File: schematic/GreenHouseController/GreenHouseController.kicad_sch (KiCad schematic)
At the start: 7 parts, among them J1 Conn_01x05, J2 Conn_01x02, J3 Conn_01x02, Q1 AO3400A, Q2 AO3400A, U1 ESP32-WROOM-32

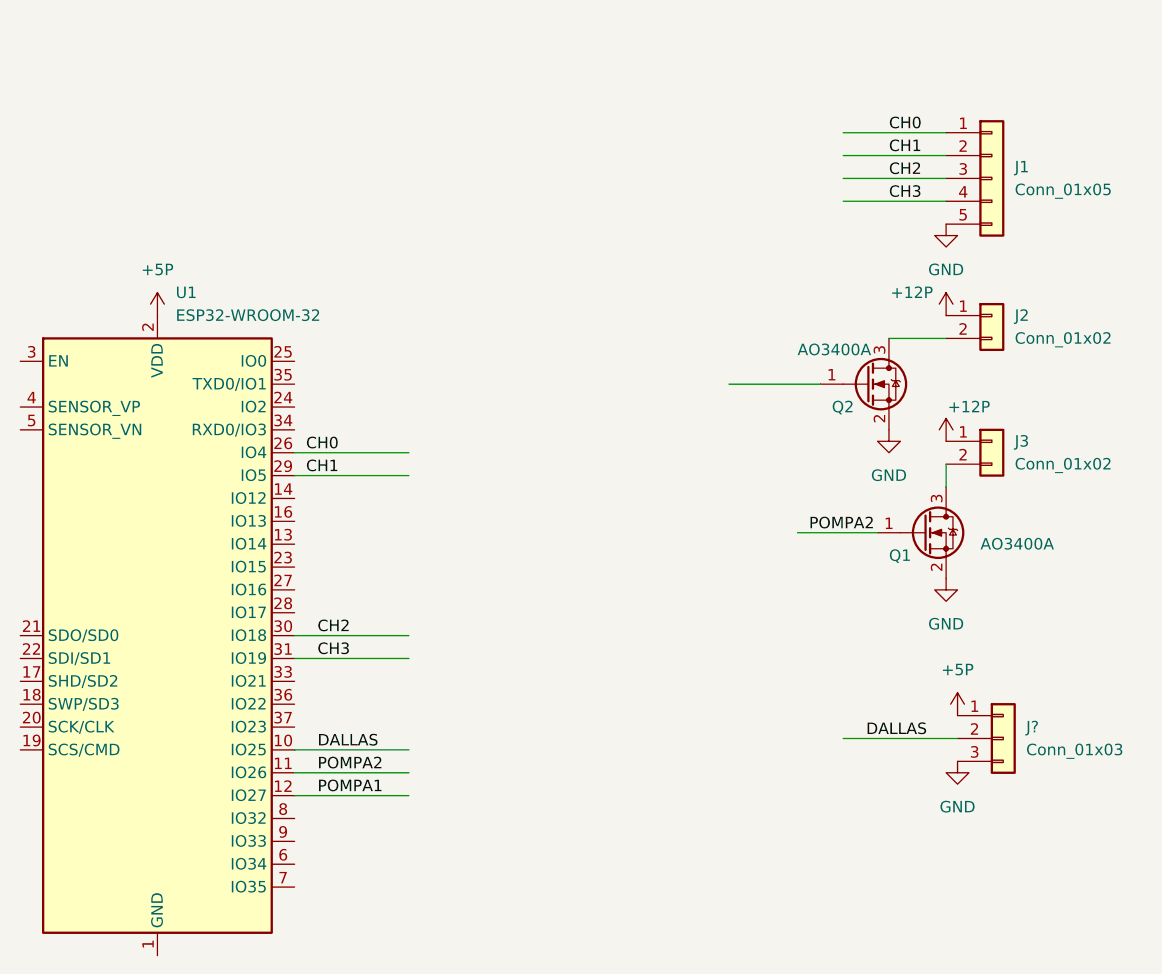
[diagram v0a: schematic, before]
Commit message: Inverted CH0-4 signals
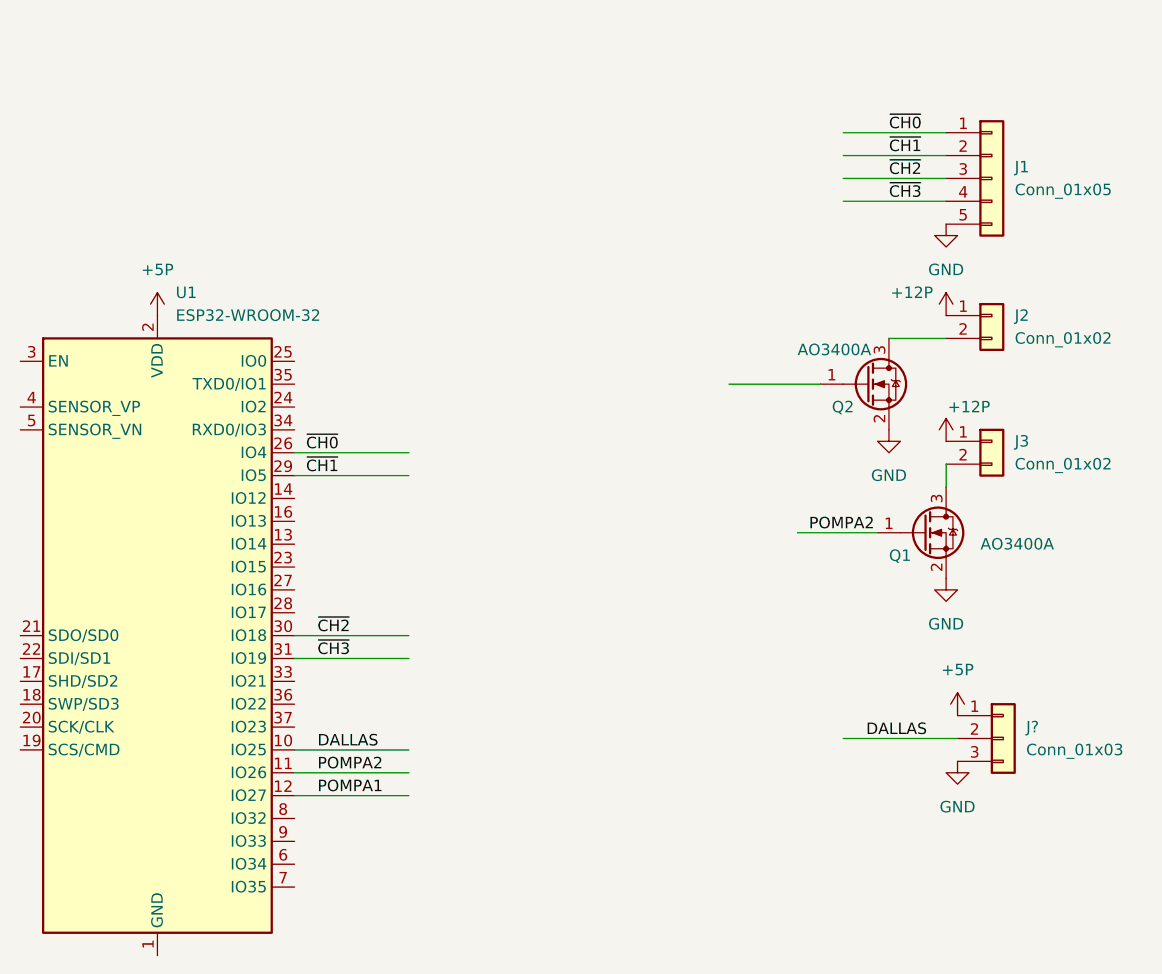
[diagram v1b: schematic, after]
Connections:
- net CH0 renamed ~{CH0}
- net CH1 renamed ~{CH1}
- net CH2 renamed ~{CH2}
- net CH3 renamed ~{CH3}
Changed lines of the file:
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@@
     (effects (font (size 1.27 1.27)) (justify left bottom))
   )
-  (label "CH3" (at 118.11 85.09 0)
+  (label "~{CH3}" (at 118.11 85.09 0)
     (effects (font (size 1.27 1.27)) (justify left bottom))
   )
@@
     (effects (font (size 1.27 1.27)) (justify left bottom))
   )
-  (label "CH0" (at 181.61 26.67 0)
+  (label "~{CH0}" (at 181.61 26.67 0)
     (effects (font (size 1.27 1.27)) (justify left bottom))
   )
-  (label "CH0" (at 116.84 62.23 0)
+  (label "~{CH0}" (at 116.84 62.23 0)
     (effects (font (size 1.27 1.27)) (justify left bottom))
   )
-  (label "CH3" (at 181.61 34.29 0)
+  (label "~{CH3}" (at 181.61 34.29 0)
     (effects (font (size 1.27 1.27)) (justify left bottom))
   )
-  (label "CH2" (at 181.61 31.75 0)
+  (label "~{CH2}" (at 181.61 31.75 0)
     (effects (font (size 1.27 1.27)) (justify left bottom))
   )
@@
     (effects (font (size 1.27 1.27)) (justify left bottom))
   )
-  (label "CH2" (at 118.11 82.55 0)
+  (label "~{CH2}" (at 118.11 82.55 0)
     (effects (font (size 1.27 1.27)) (justify left bottom))
   )
-  (label "CH1" (at 181.61 29.21 0)
+  (label "~{CH1}" (at 181.61 29.21 0)
     (effects (font (size 1.27 1.27)) (justify left bottom))
   )
@@
     (effects (font (size 1.27 1.27)) (justify left bottom))
   )
-  (label "CH1" (at 116.84 64.77 0)
+  (label "~{CH1}" (at 116.84 64.77 0)
     (effects (font (size 1.27 1.27)) (justify left bottom))
   )

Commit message: work in progress
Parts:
- added J?: Conn_01x05, symbol Connector_Generic:Conn_01x05
- renumbered J1 to MOST1
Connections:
- net GND: now also J?.1 (Pin_1)
- net SPI_CLK: now reaches U1.13 (IO14)
- net SPI_CLK: now also J?.2 (Pin_2)
- net SPI_MISO: now reaches U1.14 (IO12)
- net SPI_MISO: now also J?.3 (Pin_3)
- net SPI_MOSI: now reaches U1.16 (IO13)
- net MOIST1_CS: now reaches U1.23 (IO15)
- net MOIST1_CS: now also J?.4 (Pin_4)
- net MOIST2_CS: now reaches U1.24 (IO2)
- new net +5V: J?.5 (Pin_5)
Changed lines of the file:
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@@
+    (stroke (width 0) (type default) (color 0 0 0 0))
+  )
+  (wire (pts (xy 115.57 57.15) (xy 128.27 57.15))
+    (stroke (width 0) (type default) (color 0 0 0 0))
+  )
+  (wire (pts (xy 115.57 74.93) (xy 128.27 74.93))
+    (stroke (width 0) (type default) (color 0 0 0 0))
+  )
+  (wire (pts (xy 144.78 35.56) (xy 144.78 40.64))
     (stroke (width 0) (type default) (color 0 0 0 0))
   )
@@
     (stroke (width 0) (type default) (color 0 0 0 0))
   )
+  (wire (pts (xy 132.08 27.94) (xy 144.78 27.94))
+    (stroke (width 0) (type default) (color 0 0 0 0))
+  )
   (wire (pts (xy 171.45 71.12) (xy 180.34 71.12))
     (stroke (width 0) (type default) (color 0 0 0 0))
   )
+  (wire (pts (xy 132.08 33.02) (xy 144.78 33.02))
+    (stroke (width 0) (type default) (color 0 0 0 0))
+  )
+  (wire (pts (xy 115.57 67.31) (xy 128.27 67.31))
+    (stroke (width 0) (type default) (color 0 0 0 0))
+  )
   (wire (pts (xy 115.57 95.25) (xy 128.27 95.25))
     (stroke (width 0) (type default) (color 0 0 0 0))
   )
+  (wire (pts (xy 115.57 72.39) (xy 128.27 72.39))
+    (stroke (width 0) (type default) (color 0 0 0 0))
+  )
   (wire (pts (xy 181.61 49.53) (xy 187.96 49.53))
     (stroke (width 0) (type default) (color 0 0 0 0))
   )
+  (wire (pts (xy 115.57 69.85) (xy 128.27 69.85))
+    (stroke (width 0) (type default) (color 0 0 0 0))
+  )
+  (wire (pts (xy 144.78 20.32) (xy 144.78 25.4))
+    (stroke (width 0) (type default) (color 0 0 0 0))
+  )
+  (wire (pts (xy 132.08 30.48) (xy 144.78 30.48))
+    (stroke (width 0) (type default) (color 0 0 0 0))
+  )
   (wire (pts (xy 115.57 97.79) (xy 128.27 97.79))
     (stroke (width 0) (type default) (color 0 0 0 0))
@@
     (effects (font (size 1.27 1.27)) (justify left bottom))
   )
+  (label "SPI_MISO" (at 116.84 67.31 0)
+    (effects (font (size 1.27 1.27)) (justify left bottom))
+  )
   (label "~{CH3}" (at 118.11 85.09 0)
     (effects (font (size 1.27 1.27)) (justify left bottom))
   )
+  (label "SPI_CLK" (at 116.84 72.39 0)
+    (effects (font (size 1.27 1.27)) (justify left bottom))
+  )
+  (label "MOIST1_CS" (at 133.35 33.02 0)
+    (effects (font (size 1.27 1.27)) (justify left bottom))
+  )
+  (label "MOIST1_CS" (at 116.84 74.93 0)
+    (effects (font (size 1.27 1.27)) (justify left bottom))
+  )
   (label "DALLAS" (at 179.07 93.98 0)
     (effects (font (size 1.27 1.27)) (justify left bottom))
   )
+  (label "SPI_MOSI" (at 116.84 69.85 0)
+    (effects (font (size 1.27 1.27)) (justify left bottom))
+  )
   (label "~{CH0}" (at 181.61 26.67 0)
     (effects (font (size 1.27 1.27)) (justify left bottom))
@@
     (effects (font (size 1.27 1.27)) (justify left bottom))
   )
+  (label "SPI_CLK" (at 133.35 27.94 0)
+    (effects (font (size 1.27 1.27)) (justify left bottom))
+  )
   (label "~{CH2}" (at 181.61 31.75 0)
     (effects (font (size 1.27 1.27)) (justify left bottom))
@@
     (effects (font (size 1.27 1.27)) (justify left bottom))
   )
+  (label "SPI_MISO" (at 133.35 30.48 0)
+    (effects (font (size 1.27 1.27)) (justify left bottom))
+  )
   (label "~{CH2}" (at 118.11 82.55 0)
+    (effects (font (size 1.27 1.27)) (justify left bottom))
+  )
+  (label "MOIST2_CS" (at 116.84 57.15 0)
     (effects (font (size 1.27 1.27)) (justify left bottom))
   )
@@
     (pin "1")
   )
+  (symbol (lib_id "power:GND") (at 144.78 20.32 180) (unit 1)
+    (in_bom yes) (on_board yes) (fields_autoplaced)
+    (property "Reference" "#PWR?" (id 0) (at 144.78 13.97 0)
+      (effects (font (size 1.27 1.27)) hide)
+    )
+    (property "Value" "GND" (id 1) (at 144.78 15.24 0))
+    (property "Footprint" "" (id 2) (at 144.78 20.32 0)
+      (effects (font (size 1.27 1.27)) hide)
+    )
+    (property "Datasheet" "" (id 3) (at 144.78 20.32 0)
+      (effects (font (size 1.27 1.27)) hide)
+    )
+    (pin "1")
+  )
   (symbol (lib_id "Connector_Generic:Conn_01x02") (at 193.04 46.99 0) (unit 1)
     (in_bom yes) (on_board yes) (fields_autoplaced)
@@
     (pin "1")
   )
+  (symbol (lib_id "power:+5V") (at 144.78 40.64 0) (mirror x) (unit 1)
+    (in_bom yes) (on_board yes) (fields_autoplaced)
+    (property "Reference" "#PWR?" (id 0) (at 144.78 36.83 0)
+      (effects (font (size 1.27 1.27)) hide)
+    )
+    (property "Value" "+5V" (id 1) (at 144.78 45.72 0))
+    (property "Footprint" "" (id 2) (at 144.78 40.64 0)
+      (effects (font (size 1.27 1.27)) hide)
+    )
+    (property "Datasheet" "" (id 3) (at 144.78 40.64 0)
+      (effects (font (size 1.27 1.27)) hide)
+    )
+    (pin "1")
+  )
   (symbol (lib_id "power:+12P") (at 187.96 46.99 0) (unit 1)
     (in_bom yes) (on_board yes)
@@
   (symbol (lib_id "Connector_Generic:Conn_01x05") (at 193.04 31.75 0) (unit 1)
     (in_bom yes) (on_board yes) (fields_autoplaced)
-    (property "Reference" "J1" (id 0) (at 195.58 30.4799 0)
+    (property "Reference" "MOST1" (id 0) (at 195.58 30.4799 0)
       (effects (font (size 1.27 1.27)) (justify left))
     )
@@
     (pin "3")
   )
+  (symbol (lib_id "Connector_Generic:Conn_01x05") (at 149.86 30.48 0) (unit 1)
+    (in_bom yes) (on_board yes) (fields_autoplaced)
+    (property "Reference" "J?" (id 0) (at 152.4 29.2099 0)
+      (effects (font (size 1.27 1.27)) (justify left))
+    )
+    (property "Value" "Conn_01x05" (id 1) (at 152.4 31.7499 0)
+      (effects (font (size 1.27 1.27)) (justify left))
+    )
+    (property "Footprint" "" (id 2) (at 149.86 30.48 0)
+      (effects (font (size 1.27 1.27)) hide)
+    )
+    (property "Datasheet" "~" (id 3) (at 149.86 30.48 0)
+      (effects (font (size 1.27 1.27)) hide)
+    )
+    (pin "1")
+    (pin "2")
+    (pin "3")
+    (pin "4")
+    (pin "5")
+  )
   (symbol (lib_id "Connector_Generic:Conn_01x03") (at 194.31 93.98 0) (unit 1)
     (in_bom yes) (on_board yes) (fields_autoplaced)
@@
       (reference "#PWR?") (unit 1) (value "+12P") (footprint "")
     )
+    (path "/299405f9-a8da-40aa-a785-951754bc9be1"
+      (reference "#PWR?") (unit 1) (value "GND") (footprint "")
+    )
     (path "/640bd502-d895-424c-8932-8ffe795a3c95"
       (reference "#PWR?") (unit 1) (value "+5P") (footprint "")
     )
+    (path "/7e6cef86-5304-43b4-a13e-c8be103e805f"
+      (reference "#PWR?") (unit 1) (value "+5V") (footprint "")
+    )
     (path "/84fee7d1-65d3-477d-b1b9-fa7707645a28"
       (reference "#PWR?") (unit 1) (value "+12P") (footprint "")
@@
       (reference "#PWR?") (unit 1) (value "GND") (footprint "")
     )
-    (path "/9b774066-2c22-4032-af01-4291adb02340"
-      (reference "J1") (unit 1) (value "Conn_01x05") (footprint "")
-    )
     (path "/3cfb8fa1-01dc-43eb-be74-63e3c2902364"
       (reference "J2") (unit 1) (value "Conn_01x02") (footprint "")
@@
       (reference "J3") (unit 1) (value "Conn_01x02") (footprint "")
     )
+    (path "/efca2809-2036-46b8-8545-a5bdd08b5301"
+      (reference "J?") (unit 1) (value "Conn_01x05") (footprint "")
+    )
     (path "/fcb3a8d6-3253-4fec-933d-7cda8b97b642"
       (reference "J?") (unit 1) (value "Conn_01x03") (footprint "")
     )
+    (path "/9b774066-2c22-4032-af01-4291adb02340"
+      (reference "MOST1") (unit 1) (value "Conn_01x05") (footprint "")
+    )
     (path "/45817af6-c058-44a0-8969-3b94799d8381"
